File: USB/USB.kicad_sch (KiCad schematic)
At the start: 38 parts, among them IC1 TXS0202YZPR, IC2 NCV8730ASN330T1G, IC3 TXS0202YZPR, J1 MISC1, U1 TLV61222

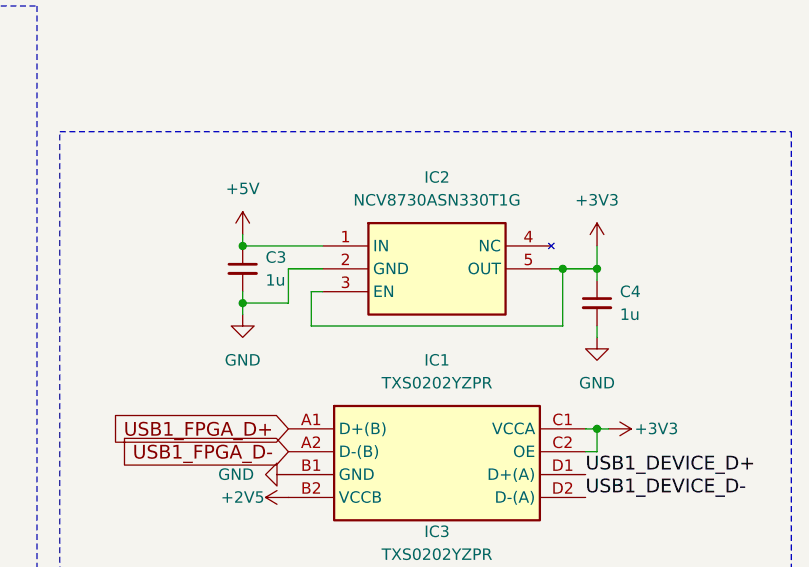
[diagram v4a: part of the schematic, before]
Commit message: Fix #6
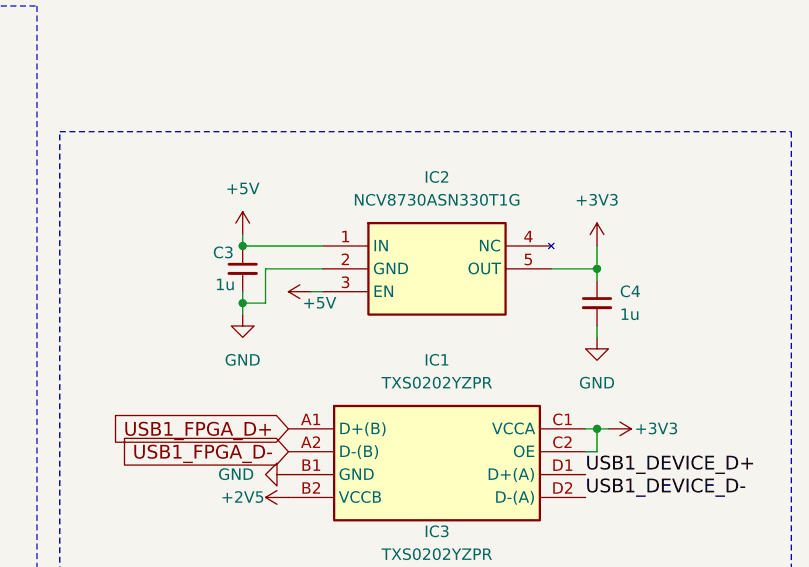
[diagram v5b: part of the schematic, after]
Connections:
- net +3V3: no longer IC2.3 (EN)
- net +5V: now also IC2.3 (EN)
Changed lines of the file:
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@@
 	)
 	(junction
-		(at 247.65 106.68)
-		(diameter 0)
-		(color 0 0 0 0)
-	)
-	(junction
 		(at 71.12 140.97)
 		(diameter 0)
@@
 	(wire
 		(pts
-			(xy 251.46 106.68) (xy 247.65 106.68)
+			(xy 246.38 106.68) (xy 251.46 106.68)
 		)
 		(stroke
@@
 	(wire
 		(pts
-			(xy 247.65 106.68) (xy 246.38 106.68)
-		)
-		(stroke
-			(width 0)
-			(type default)
-		)
-	)
-	(wire
-		(pts
 			(xy 158.75 120.65) (xy 158.75 125.73)
 		)
@@
 	(wire
 		(pts
-			(xy 219.71 113.03) (xy 247.65 113.03)
-		)
-		(stroke
-			(width 0)
-			(type default)
-		)
-	)
-	(wire
-		(pts
 			(xy 158.75 140.97) (xy 163.83 140.97)
 		)
@@
 	(wire
 		(pts
-			(xy 217.17 106.68) (xy 217.17 110.49)
+			(xy 214.63 106.68) (xy 214.63 110.49)
 		)
 		(stroke
@@
 	(wire
 		(pts
-			(xy 219.71 109.22) (xy 219.71 113.03)
-		)
-		(stroke
-			(width 0)
-			(type default)
-		)
-	)
-	(wire
-		(pts
 			(xy 251.46 143.51) (xy 250.19 143.51)
 		)
@@
 	(wire
 		(pts
-			(xy 212.09 110.49) (xy 217.17 110.49)
+			(xy 212.09 110.49) (xy 214.63 110.49)
 		)
 		(stroke
@@
 	(wire
 		(pts
-			(xy 220.98 106.68) (xy 217.17 106.68)
+			(xy 220.98 106.68) (xy 214.63 106.68)
 		)
 		(stroke
@@
 	(wire
 		(pts
-			(xy 247.65 106.68) (xy 247.65 113.03)
-		)
-		(stroke
-			(width 0)
-			(type default)
-		)
-	)
-	(wire
-		(pts
 			(xy 143.51 93.98) (xy 153.67 93.98)
 		)
@@
 		(on_board yes)
 		(dnp no)
-		(fields_autoplaced yes)
 		(property "Reference" "C3"
-			(at 214.63 105.4162 0)
+			(at 208.788 104.902 0)
 			(effects
 				(font
@@
 		)
 		(property "Value" "1u"
-			(at 214.63 107.9562 0)
+			(at 209.042 108.458 0)
 			(effects
 				(font
@@
 					(unit 1)
 				)
+			)
+		)
+	)
+	(symbol
+		(lib_name "+5V_1")
+		(lib_id "power:+5V")
+		(at 219.71 109.22 90)
+		(unit 1)
+		(exclude_from_sim no)
+		(in_bom yes)
+		(on_board yes)
+		(dnp no)
+		(property "Reference" "#PWR030"
+			(at 223.52 109.22 0)
+			(effects
+				(font
+					(size 1.27 1.27)
+				)
+				(hide yes)
+			)
+		)
+		(property "Value" "+5V"
+			(at 222.504 110.49 90)
+			(effects
+				(font
+					(size 1.27 1.27)
+				)
+				(justify left)
+			)
+		)
+		(property "Footprint" ""
+			(at 219.71 109.22 0)
+			(effects
+				(font
+					(size 1.27 1.27)
+				)
+				(hide yes)
+			)
+		)
+		(property "Datasheet" ""
+			(at 219.71 109.22 0)
+			(effects
+				(font
+					(size 1.27 1.27)
+				)
+				(hide yes)
+			)
+		)
+		(property "Description" "Power symbol creates a global label with name \"+5V\""
+			(at 219.71 109.22 0)
+			(effects
+				(font
+					(size 1.27 1.27)
+				)
+				(hide yes)
+			)
+		)
+		(pin "1"
+		)
+		(instances
+			(project "USB"
+				(path "/7fff477f-def8-4fe2-9475-2ccc11474981"
+					(reference "#PWR030")
+					(unit 1)
+				)
